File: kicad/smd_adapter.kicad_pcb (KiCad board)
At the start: 2 copper layers, 76.4 x 71.2 mm, 27 parts

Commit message: Added a tssop 20 footprint
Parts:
- added REF**: SMD_ADAPTER_TSSOP-20, smd_adapter:SMD_ADAPTER_TSSOP-20, F.Cu at (164.3, 39.2)
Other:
- board size 76.4 x 71.2 mm -> 105 x 71.2 mm

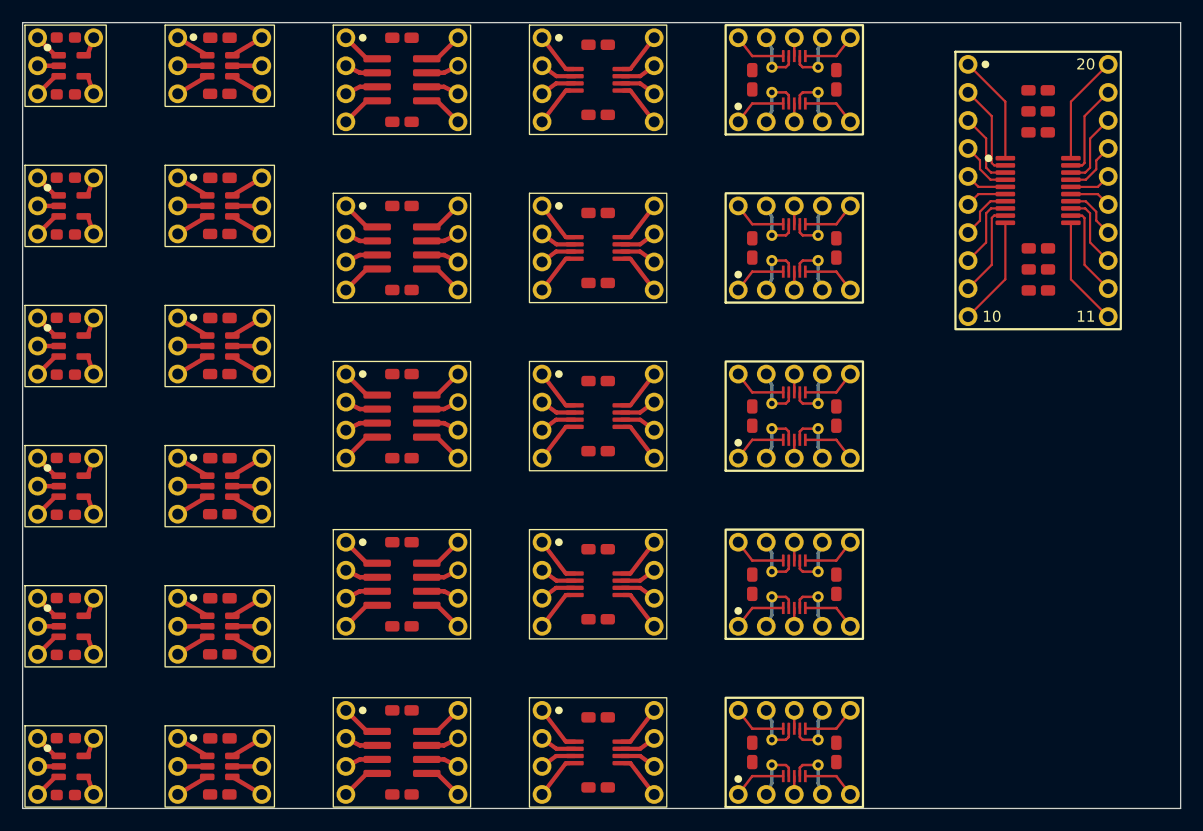
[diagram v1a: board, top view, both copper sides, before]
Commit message: Cleaned up the layout and added a few footprints.
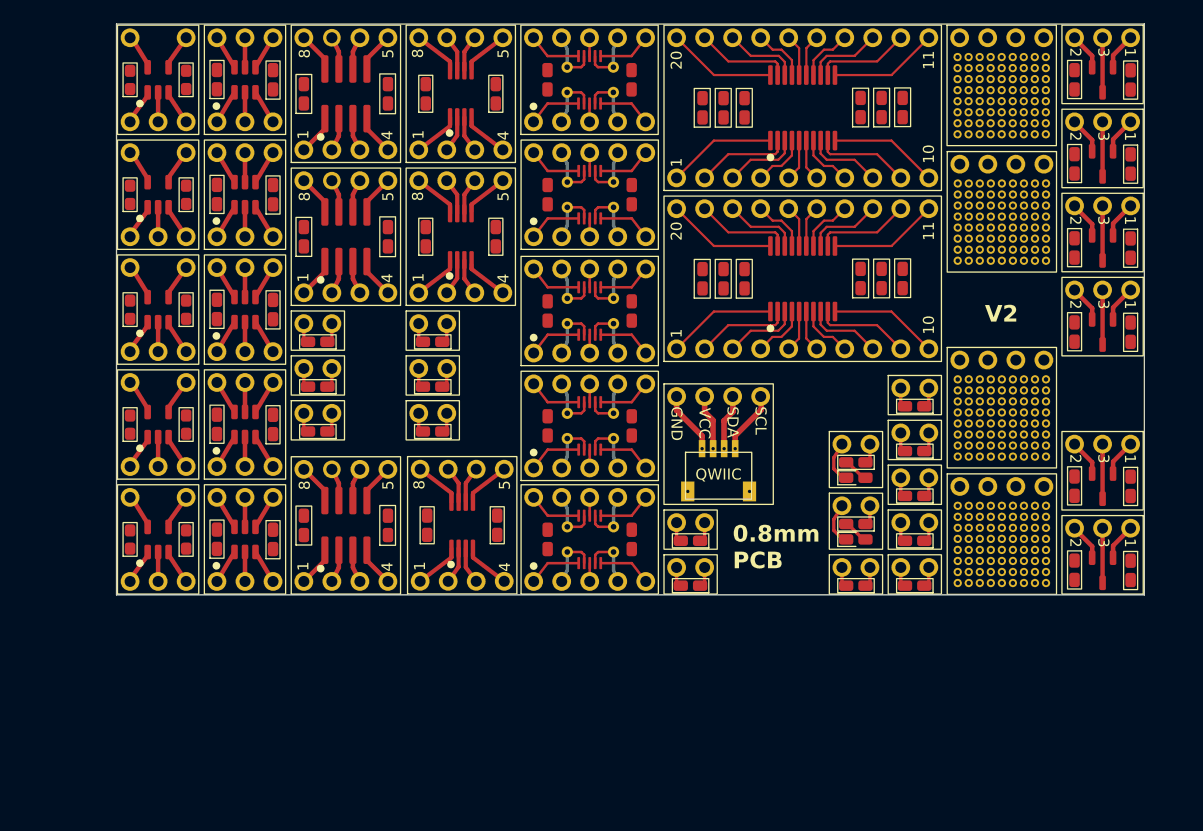
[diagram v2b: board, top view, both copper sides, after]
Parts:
- removed the REF** at (76.8, 40.6)
- removed the REF** at (90.2, 66.0)
- removed the REF** at (90.2, 40.6)
- removed the REF** at (142.2, 59.7)
- removed the REF** at (142.2, 90.2)
- removed the REF** at (106.7, 90.2)
- removed the REF** at (106.7, 74.9)
- removed the REF** at (124.5, 59.7)
- removed the REF** at (90.2, 78.7)
- removed the REF** at (142.2, 74.9)
- removed the REF** at (124.5, 44.5)
- removed the REF** at (90.2, 91.4)
- removed the REF** at (124.5, 90.2)
- removed the REF** at (90.2, 53.3)
- removed the REF** at (142.2, 44.5)
- removed the REF** at (124.5, 74.9)
- removed the REF** at (106.7, 44.5)
- removed the REF** at (106.7, 59.7)
- added REF**: SMD_ADAPTER_SOIC-8, smd_adapter:SMD_ADAPTER_SOIC-8, F.Cu at (101.6, 69.6)
- added REF**: SMD_ADAPTER_R, smd_adapter:SMD_ADAPTER_R, F.Cu at (109.5, 55.4)
- added REF**: QWIIC_adapter, smd_adapter:SMD_ADAPTER_GRID, F.Cu at (161.1, 36.9)
- added REF**: SMD_ADAPTER_SOT-23-3, smd_adapter:SMD_ADAPTER_SOT-23-3, F.Cu at (170.2, 44.5)
- added REF**: SMD_ADAPTER_R, smd_adapter:SMD_ADAPTER_R, F.Cu at (109.5, 51.3)
- added REF**: SMD_ADAPTER_R, smd_adapter:SMD_ADAPTER_R, F.Cu at (99.1, 59.4)
- added REF**: SMD_ADAPTER_R, smd_adapter:SMD_ADAPTER_R, F.Cu at (132.8, 73.4)
- added REF**: SMD_ADAPTER_LED, smd_adapter:SMD_ADAPTER_LED, F.Cu at (147.8, 62.2)
- added REF**: SMD_ADAPTER_TSSOP-10, smd_adapter:SMD_ADAPTER_TSSOP-10, F.Cu at (123.7, 70.9)
- added REF**: SMD_ADAPTER_R, smd_adapter:SMD_ADAPTER_R, F.Cu at (153.2, 61.2)
- added REF**: SMD_ADAPTER_TSSOP-10, smd_adapter:SMD_ADAPTER_TSSOP-10, F.Cu at (123.7, 60.6)
- added REF**: SMD_ADAPTER_R, smd_adapter:SMD_ADAPTER_R, F.Cu at (153.2, 57.1)
- added REF**: SMD_ADAPTER_R, smd_adapter:SMD_ADAPTER_R, F.Cu at (132.8, 69.3)
- added REF**: SMD_ADAPTER_SOT-23-6, smd_adapter:SMD_ADAPTER_SOT-23-6, F.Cu at (92.5, 60.5)
- added REF**: SMD_ADAPTER_R, smd_adapter:SMD_ADAPTER_R, F.Cu at (153.2, 69.3)
- added REF**: SMD_ADAPTER_SOT-23-3, smd_adapter:SMD_ADAPTER_SOT-23-3, F.Cu at (170.2, 36.8)
- added REF**: SMD_ADAPTER_TSSOP-10, smd_adapter:SMD_ADAPTER_TSSOP-10, F.Cu at (123.7, 50.2)
- added REF**: SMD_ADAPTER_TSSOP-10, smd_adapter:SMD_ADAPTER_TSSOP-10, F.Cu at (123.7, 39.6)
- added REF**: QWIIC_adapter, smd_adapter:SMD_ADAPTER_QWIIC_connector, F.Cu at (135.4, 57.9)
- added REF**: SMD_ADAPTER_SOT-23-6, smd_adapter:SMD_ADAPTER_SOT-23-6, F.Cu at (92.5, 70.9)
- added REF**: SMD_ADAPTER_LED, smd_adapter:SMD_ADAPTER_LED, F.Cu at (147.8, 67.8)
- added REF**: SMD_ADAPTER_SOT-23-3, smd_adapter:SMD_ADAPTER_SOT-23-3, F.Cu at (170.2, 73.7)
- added REF**: QWIIC_adapter, smd_adapter:SMD_ADAPTER_GRID, F.Cu at (161.1, 66.1)
- added REF**: SMD_ADAPTER_SOT-23-3, smd_adapter:SMD_ADAPTER_SOT-23-3, F.Cu at (170.2, 52.1)
- added REF**: SMD_ADAPTER_R, smd_adapter:SMD_ADAPTER_R, F.Cu at (147.8, 73.4)
- added REF**: QWIIC_adapter, smd_adapter:SMD_ADAPTER_GRID, F.Cu at (161.0, 25.4)
- added REF**: QWIIC_adapter, smd_adapter:SMD_ADAPTER_GRID, F.Cu at (161.1, 54.6)
- added REF**: SMD_ADAPTER_MSOP-8, smd_adapter:SMD_ADAPTER_MSOP-8, F.Cu at (112.1, 69.6)
- added REF**: SMD_ADAPTER_R, smd_adapter:SMD_ADAPTER_R, F.Cu at (153.2, 73.4)
- added REF**: SMD_ADAPTER_R, smd_adapter:SMD_ADAPTER_R, F.Cu at (109.5, 59.4)
- added REF**: SMD_ADAPTER_SOT-23-6, smd_adapter:SMD_ADAPTER_SOT-23-6, F.Cu at (92.5, 39.6)
- added REF**: SMD_ADAPTER_TSSOP-20, smd_adapter:SMD_ADAPTER_TSSOP-20, F.Cu at (143.0, 47.2)
- added REF**: SMD_ADAPTER_R, smd_adapter:SMD_ADAPTER_R, F.Cu at (153.2, 65.3)
- added REF**: SMD_ADAPTER_MSOP-8, smd_adapter:SMD_ADAPTER_MSOP-8, F.Cu at (112.0, 43.4)
- added REF**: SMD_ADAPTER_SOIC-8, smd_adapter:SMD_ADAPTER_SOIC-8, F.Cu at (101.6, 43.4)
- added REF**: SMD_ADAPTER_SOT-23-3, smd_adapter:SMD_ADAPTER_SOT-23-3, F.Cu at (170.2, 29.2)
- added REF**: SMD_ADAPTER_R, smd_adapter:SMD_ADAPTER_R, F.Cu at (99.1, 51.3)
- added REF**: SMD_ADAPTER_SOT-23-3, smd_adapter:SMD_ADAPTER_SOT-23-3, F.Cu at (170.2, 66.0)
- added REF**: SMD_ADAPTER_SOT-23-6, smd_adapter:SMD_ADAPTER_SOT-23-6, F.Cu at (92.5, 50.0)
- added REF**: SMD_ADAPTER_R, smd_adapter:SMD_ADAPTER_R, F.Cu at (99.1, 55.4)
- moved REF** 22.6 mm to (143.0, 31.8), turned to 90 degrees
- moved REF** 22.0 mm to (84.6, 70.9), turned to 90 degrees
- moved REF** 19.9 mm to (84.6, 60.5), turned to 90 degrees
- moved REF** 18.6 mm to (123.7, 29.2)
- moved REF** 17.8 mm to (84.6, 50.0), turned to 90 degrees
- moved REF** 15.8 mm to (84.6, 39.6), turned to 90 degrees
- moved REF** 12.5 mm to (112.0, 30.5), turned to 90 degrees
- moved REF** 7.85 mm to (84.6, 29.2), turned to 90 degrees
- moved REF** 5.24 mm to (101.6, 30.5), turned to 90 degrees
- moved REF** 2.62 mm to (92.5, 29.2), turned to 90 degrees
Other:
- board size 105 x 71.2 mm -> 93.2 x 51.7 mm
- board text added: "* Place on a 10mil grid. * Each footprint width/length should be a multiplier of 10mil * 20mil spacing between borders of adjustent footprints (center to center) * Cut vertical stripes and then horizontally."
- board text added: "0.8mm PCB"
- board text added: "V2"

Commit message: Tweaked the QWIIC smd adapter.
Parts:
- added REF**: SMD_ADAPTER_R, smd_adapter:SMD_ADAPTER_R, F.Cu at (132.8, 58.2)
- added REF**: SMD_ADAPTER_R, smd_adapter:SMD_ADAPTER_R, F.Cu at (163.6, 50.4)
- REF**: footprint smd_adapter:SMD_ADAPTER_QWIIC_connector -> smd_adapter:SMD_ADAPTER_QWIIC
- moved REF** 40.2 mm to (171.4, 58.2)
- moved REF** 21.4 mm to (147.8, 58.2)
- moved REF** 4.32 mm to (135.4, 62.2)
